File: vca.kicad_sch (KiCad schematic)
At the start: 65 parts, among them J1 Signal 1, J2 Signal 2, J3 CV 1, J4 CV 2, J5 Out 1, J6 Out 2, J7 Conn_02x05_Odd_Even, Q1 BCM847, Q2 BC547C, U1 TL074

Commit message: prepping for initial manu
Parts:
- added TP1: TestPoint, TestPoint:TestPoint_Plated_Hole_D2.0mm, symbol Connector:TestPoint
- D1, D2: PartNum (none) -> 863-BAT54SLT1G; Vendor (none) -> Mouser
- H1, H10, H11, H12, H13, H14, H2, H3, H4, H5, H7, H8, H9: now left out of the parts list
- H6: symbol Mechanical:MountingHole_Pad -> eurorack:MountingHole_Pad_Output; now left out of the parts list
- J1, J2, J3, J4, J5, J6: PartNum (none) -> A-2566; Vendor (none) -> Tayda
- J7: PartNum (none) -> A-2939; Vendor (none) -> Tayda
- Q1: PartNum (none) -> 771-BCM847DS135; Vendor (none) -> Mouser
- Q2: PartNum (none) -> 637-BC547C; Vendor (none) -> Mouser
- RV1, RV2, RV3: PartNum (none) -> A-5407 (DC Version: A-2963); Vendor (none) -> Tayda
- RV4: PartNum (none) -> A-585; Vendor (none) -> Tayda
- RV5: PartNum (none) -> A-587; Vendor (none) -> Tayda
- RV6: PartNum (none) -> A-598; Vendor (none) -> Tayda
- U1: PartNum (none) -> 595-TL074CDR; Vendor (none) -> Mouser
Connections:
- net at R10.2, R13.2, U1.7: now also TP1.1

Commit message: v2 ready
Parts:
- removed Q2: BC547C, Package_TO_SOT_THT:TO-92L_Inline, symbol Device:Q_NPN_CBE
- added Q2, Q3: BC847C, Package_TO_SOT_SMD:SOT-23-3, symbol eurorack:BC547
- H10, H11: footprint eurorack:Mech-AudioJack-Hole -> eurorack:Mech-AudioJack-Hole-Input-CV
- H14: footprint eurorack:Mech-LED-Hole-4mm -> eurorack:Mech-LED-Hole-3mm-Bezel
- H8, H9: footprint eurorack:Mech-AudioJack-Hole -> eurorack:Mech-AudioJack-Hole-Input
- R22, R25: value 1K -> 100K
- R26: value 100 -> 1K
- RV1: value 100K LOG* -> A100K
- RV2, RV3: value 100K LOG* -> B100K
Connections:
- net +12V: now also Q3.1 (C)
- net GND: now also Q2.1 (C)
- net at R18.2, R19.2: now also Q2.2 (B)
- net at R25.2, U1.14: now also Q3.2 (B); no longer R26.2
- net at R20.2, R21.1: now also Q2.3 (E)
- new net: Q3.3 (E), R26.2
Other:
- moved on the sheet: C1, C2, C6, D3, H1, H10, H11, H12, H13, H14, H2, H3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

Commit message: correcting some BOM issues
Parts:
- Q2, Q3: value BC847C -> BC547C
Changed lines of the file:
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@@
       (effects (font (size 1.27 1.27)) (justify left))
     )
-    (property "Value" "BC847C" (at 146.05 104.14 0)
+    (property "Value" "BC547C" (at 146.05 104.14 0)
       (effects (font (size 1.27 1.27)) (justify left))
     )
@@
       (effects (font (size 1.27 1.27)) (justify left))
     )
-    (property "Value" "BC847C" (at 137.16 28.575 0)
-      (effects (font (size 1.27 1.27)) (justify left))
-    )
+    (property "Value" "BC547C" (at 137.16 28.575 0)
+      (effects (font (size 1.27 1.27)) (justify left))
+    )

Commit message: v2 actually ready for manu
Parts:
- C1, C2: value 10u* -> 10u 35V; Note (none) -> Omit and bridge pads for DC version
- D3: value LED -> LED_GREEN
- RV1: Note (none) -> Use B100K for DC version; PartNum A-5407 (DC Version: A-2963) -> (none); Vendor Tayda -> (none)
- RV2, RV3: value B100K -> A100K; Note (none) -> Use B100K for DC version; PartNum A-5407 (DC Version: A-2963) -> (none); Vendor Tayda -> (none)
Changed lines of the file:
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@@
       (effects (font (size 1.27 1.27)) (justify right))
     )
-    (property "Value" "B100K" (at 66.675 111.76 0)
+    (property "Value" "A100K" (at 66.675 111.76 0)
       (effects (font (size 1.27 1.27)) (justify right))
     )
@@
       (effects (font (size 1.27 1.27)) hide)
     )
-    (property "Vendor" "Tayda" (at 69.215 113.03 0)
-      (effects (font (size 1.27 1.27)) hide)
-    )
-    (property "PartNum" "A-5407 (DC Version: A-2963)" (at 69.215 113.03 0)
+    (property "Note" "Use B100K for DC version" (at 69.215 113.03 0)
       (effects (font (size 1.27 1.27)) hide)
     )
@@
       (effects (font (size 1.27 1.27)))
     )
-    (property "Value" "10u*" (at 79.756 58.42 90)
+    (property "Value" "10u 35V" (at 79.756 58.42 90)
       (effects (font (size 1.27 1.27)))
     )
@@
     )
     (property "Datasheet" "~" (at 80.645 63.5 0)
+      (effects (font (size 1.27 1.27)) hide)
+    )
+    (property "Note" "Omit and bridge pads for DC version" (at 80.645 63.5 90)
       (effects (font (size 1.27 1.27)) hide)
     )
@@
       (effects (font (size 1.27 1.27)) hide)
     )
-    (property "Vendor" "Tayda" (at 69.215 52.07 0)
-      (effects (font (size 1.27 1.27)) hide)
-    )
-    (property "PartNum" "A-5407 (DC Version: A-2963)" (at 69.215 52.07 0)
+    (property "Note" "Use B100K for DC version" (at 69.215 52.07 0)
       (effects (font (size 1.27 1.27)) hide)
     )
@@
   )
   (symbol (lib_id "Device:LED") (at 134.62 43.815 90) (unit 1)
-    (in_bom yes) (on_board yes) (dnp no) (fields_autoplaced)
+    (in_bom yes) (on_board yes) (dnp no)
     (property "Reference" "D3" (at 138.43 44.1325 90)
       (effects (font (size 1.27 1.27)) (justify right))
     )
-    (property "Value" "LED" (at 138.43 46.6725 90)
+    (property "Value" "LED_GREEN" (at 139.7 45.72 0)
       (effects (font (size 1.27 1.27)) (justify right))
     )
@@
       (effects (font (size 1.27 1.27)) (justify right))
     )
-    (property "Value" "B100K" (at 67.945 88.9 0)
+    (property "Value" "A100K" (at 67.945 88.9 0)
       (effects (font (size 1.27 1.27)) (justify right))
     )
@@
       (effects (font (size 1.27 1.27)) hide)
     )
-    (property "Vendor" "Tayda" (at 70.485 90.17 0)
-      (effects (font (size 1.27 1.27)) hide)
-    )
-    (property "PartNum" "A-5407 (DC Version: A-2963)" (at 70.485 90.17 0)
+    (property "Note" "Use B100K for DC version" (at 70.485 90.17 0)
       (effects (font (size 1.27 1.27)) hide)
     )
@@
       (effects (font (size 1.27 1.27)))
     )
-    (property "Value" "10u*" (at 79.756 46.99 90)
+    (property "Value" "10u 35V" (at 79.756 46.99 90)
       (effects (font (size 1.27 1.27)))
     )
@@
       (effects (font (size 1.27 1.27)) hide)
     )
+    (property "Note" "Omit and bridge pads for DC version" (at 80.645 52.07 90)
+      (effects (font (size 1.27 1.27)) hide)
+    )

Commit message: one last BOM issue
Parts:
- RV1, RV2, RV3: PartNum (none) -> A-5407; Vendor (none) -> Tayda
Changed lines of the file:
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@@
+      (effects (font (size 1.27 1.27)) hide)
+    )
+    (property "Vendor" "Tayda" (at 69.215 113.03 0)
+      (effects (font (size 1.27 1.27)) hide)
+    )
+    (property "PartNum" "A-5407" (at 69.215 113.03 0)
       (effects (font (size 1.27 1.27)) hide)
     )
@@
     )
     (property "Note" "Use B100K for DC version" (at 69.215 52.07 0)
+      (effects (font (size 1.27 1.27)) hide)
+    )
+    (property "Vendor" "Tayda" (at 69.215 52.07 0)
+      (effects (font (size 1.27 1.27)) hide)
+    )
+    (property "PartNum" "A-5407" (at 69.215 52.07 0)
       (effects (font (size 1.27 1.27)) hide)
     )
@@
       (effects (font (size 1.27 1.27)) hide)
     )
+    (property "Vendor" "Tayda" (at 70.485 90.17 0)
+      (effects (font (size 1.27 1.27)) hide)
+    )
+    (property "PartNum" "A-5407" (at 70.485 90.17 0)
+      (effects (font (size 1.27 1.27)) hide)
+    )

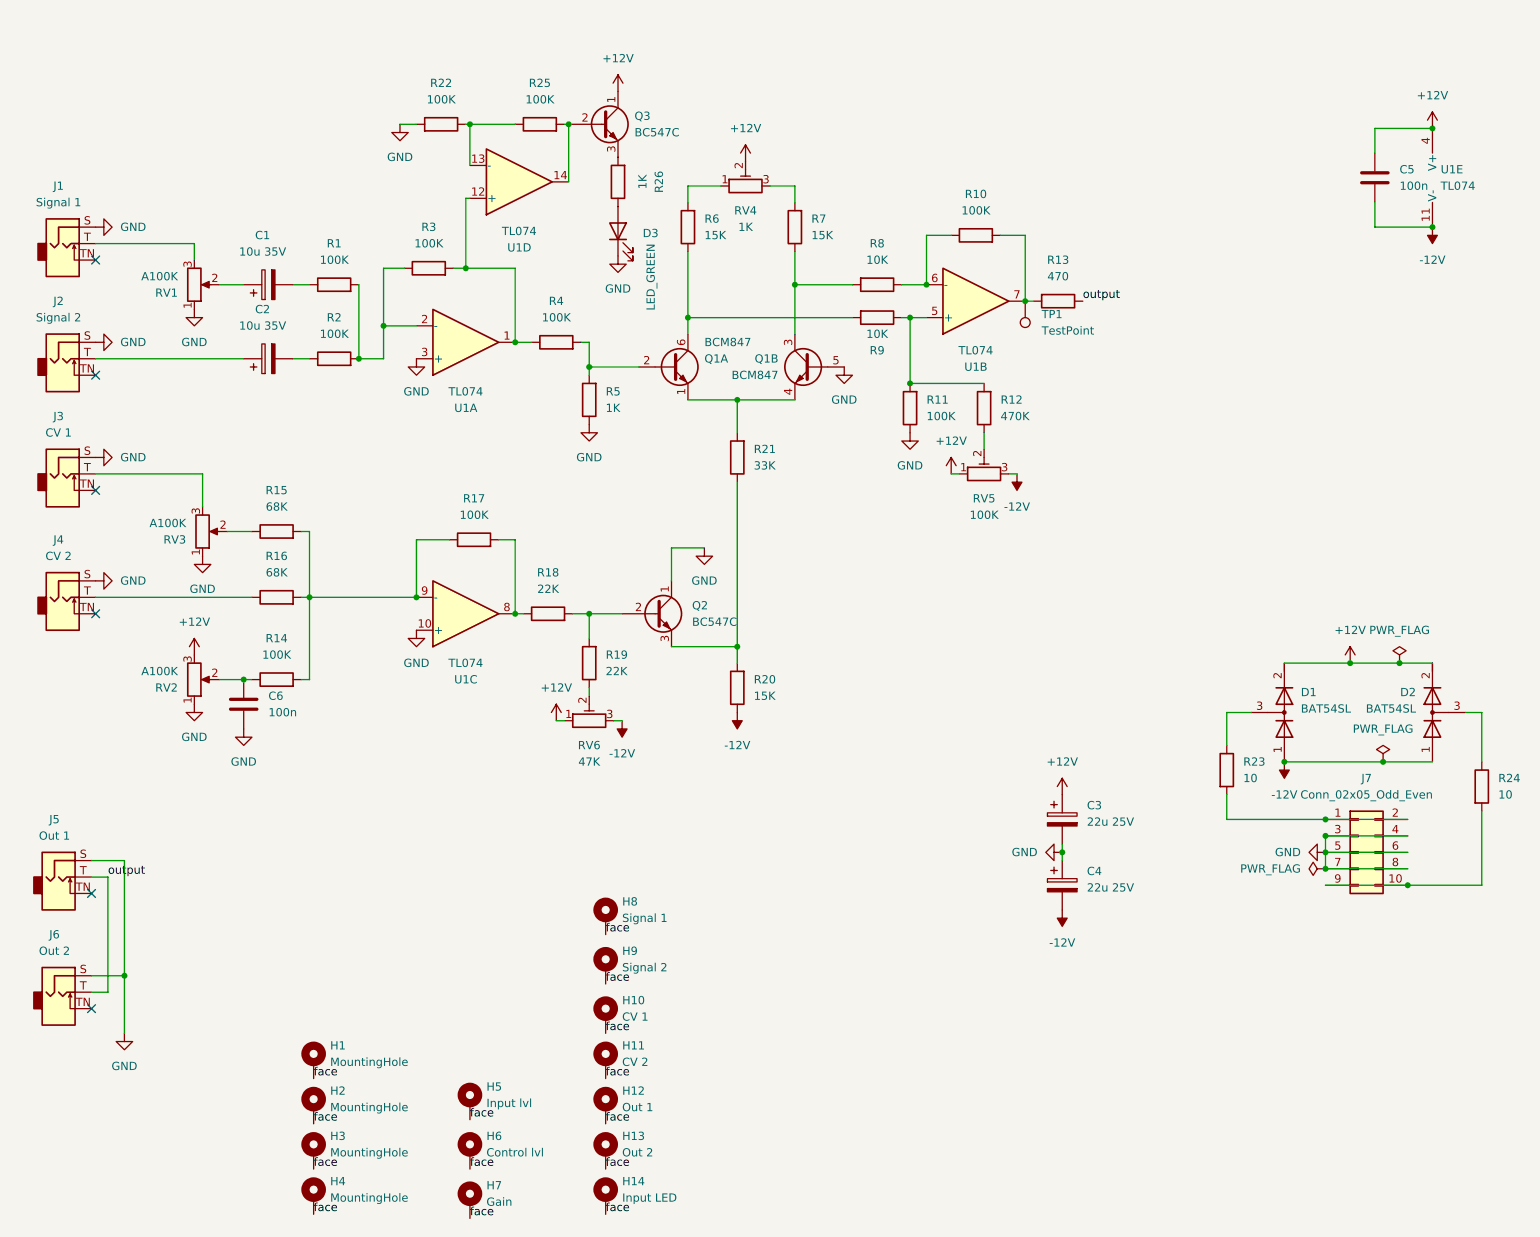
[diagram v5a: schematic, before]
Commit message: use bipolar resistor at input
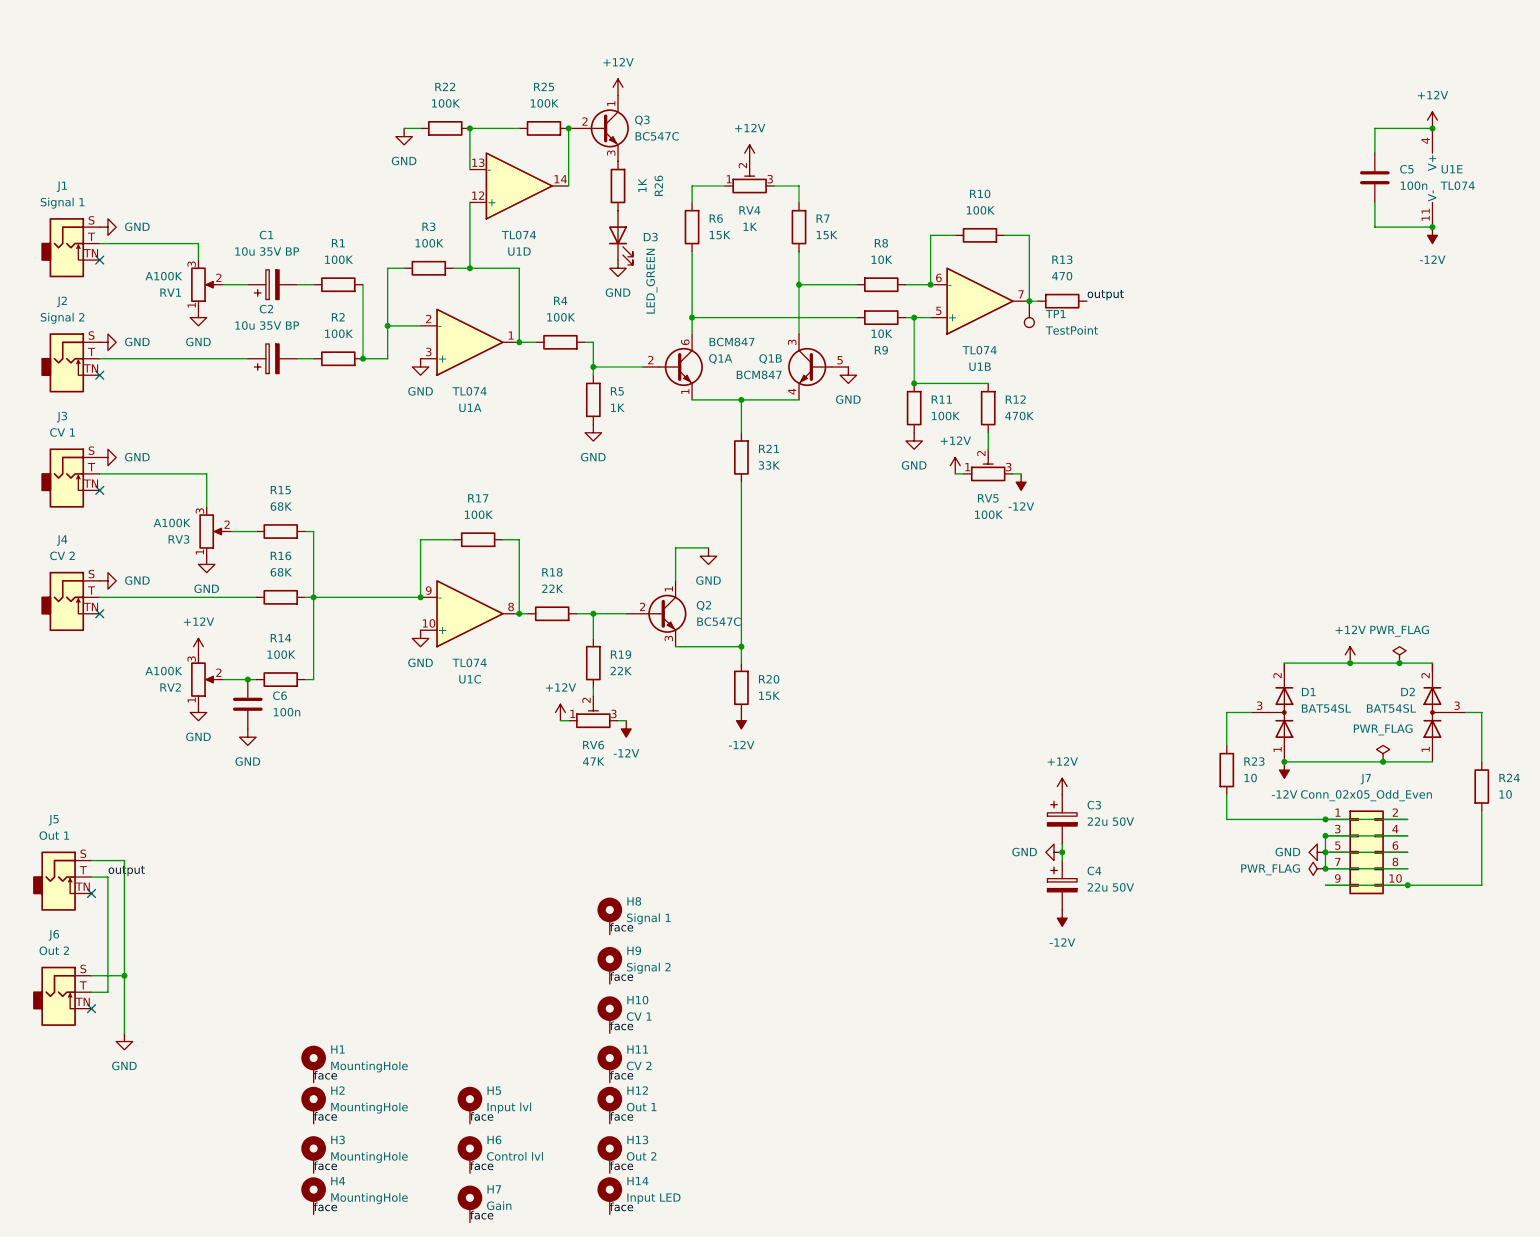
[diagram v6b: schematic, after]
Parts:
- C1, C2: value 10u 35V -> 10u 35V BP
- C3, C4: value 22u 25V -> 22u 50V
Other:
- moved on the sheet: C1, C2, C6, D3, H1, H10, H11, H12, H13, H14, H3, H5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

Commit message: bugfixes, update to kicad version 10
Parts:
- Q2, Q3: value BC547C -> BC847C; footprint Package_TO_SOT_SMD:SOT-23-3 -> Package_TO_SOT_SMD:SOT-23; symbol eurorack:BC547 -> Transistor_BJT:BC847
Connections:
- net +12V: now also Q3.3 (C); no longer Q3.1 (C)
- net GND: now also Q2.3 (C); no longer Q2.1 (C)
- net at R18.2, R19.2: now also Q2.1 (B); no longer Q2.2 (B)
- net at R20.2, R21.1: now also Q2.2 (E); no longer Q2.3 (E)
- net at R25.2, U1.14: now also Q3.1 (B); no longer Q3.2 (B)
- net at R26.2: now also Q3.2 (E); no longer Q3.3 (E)
